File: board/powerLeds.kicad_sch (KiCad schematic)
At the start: 6 parts

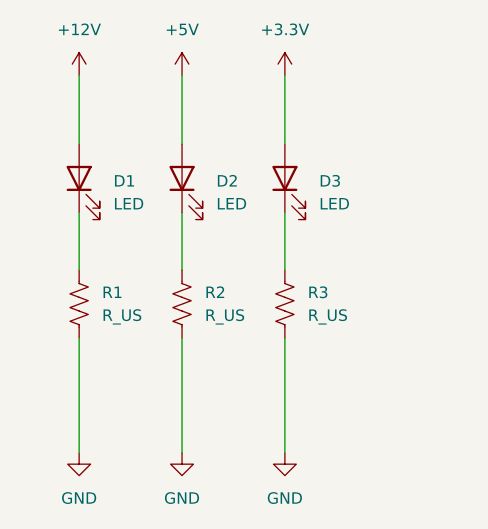
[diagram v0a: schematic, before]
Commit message: Added Resistors to Power LED's
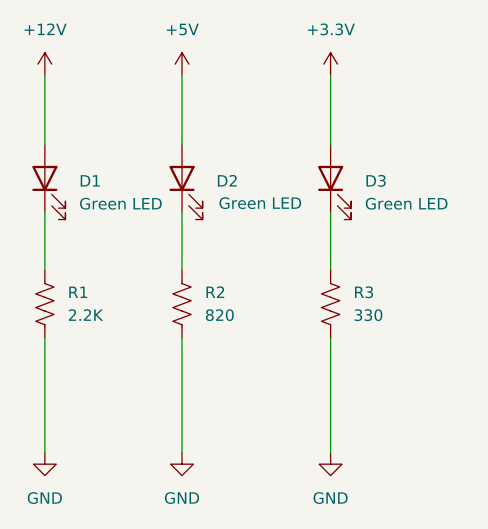
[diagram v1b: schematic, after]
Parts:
- D1, D2, D3: value LED -> Green LED
- R1: value R_US -> 2.2K
- R2: value R_US -> 820
- R3: value R_US -> 330
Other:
- moved on the sheet: D1, D3, R1, R3
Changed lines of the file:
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@@
 	(wire
 		(pts
-			(xy 127 82.55) (xy 127 90.17)
+			(xy 123.19 82.55) (xy 123.19 90.17)
 		)
 		(stroke
@@
 	(wire
 		(pts
-			(xy 127 111.76) (xy 127 124.46)
+			(xy 123.19 111.76) (xy 123.19 124.46)
 		)
 		(stroke
@@
 	(wire
 		(pts
-			(xy 149.86 97.79) (xy 149.86 104.14)
+			(xy 154.94 97.79) (xy 154.94 104.14)
 		)
 		(stroke
@@
 	(wire
 		(pts
-			(xy 149.86 82.55) (xy 149.86 90.17)
+			(xy 154.94 82.55) (xy 154.94 90.17)
 		)
 		(stroke
@@
 	(wire
 		(pts
-			(xy 149.86 111.76) (xy 149.86 124.46)
+			(xy 154.94 111.76) (xy 154.94 124.46)
 		)
 		(stroke
@@
 	(wire
 		(pts
-			(xy 127 97.79) (xy 127 104.14)
+			(xy 123.19 97.79) (xy 123.19 104.14)
 		)
 		(stroke
@@
 	(symbol
 		(lib_id "power:+12V")
-		(at 127 82.55 0)
+		(at 123.19 82.55 0)
 		(unit 1)
 		(exclude_from_sim no)
@@
 		(fields_autoplaced yes)
 		(property "Reference" "#PWR04"
-			(at 127 86.36 0)
+			(at 123.19 86.36 0)
 			(effects
 				(font
@@
 		)
 		(property "Value" "+12V"
-			(at 127 77.47 0)
-			(effects
-				(font
-					(size 1.27 1.27)
-				)
-			)
-		)
-		(property "Footprint" ""
-			(at 127 82.55 0)
+			(at 123.19 77.47 0)
+			(effects
+				(font
+					(size 1.27 1.27)
+				)
+			)
+		)
+		(property "Footprint" ""
+			(at 123.19 82.55 0)
 			(effects
 				(font
@@
 		)
 		(property "Datasheet" ""
-			(at 127 82.55 0)
+			(at 123.19 82.55 0)
 			(effects
 				(font
@@
 		)
 		(property "Description" "Power symbol creates a global label with name \"+12V\""
-			(at 127 82.55 0)
+			(at 123.19 82.55 0)
 			(effects
 				(font
@@
 	(symbol
 		(lib_id "Device:LED")
-		(at 127 93.98 90)
+		(at 123.19 93.98 90)
 		(unit 1)
 		(exclude_from_sim no)
@@
 		(fields_autoplaced yes)
 		(property "Reference" "D1"
-			(at 130.81 94.2974 90)
+			(at 127 94.2974 90)
 			(effects
 				(font
@@
 			)
 		)
-		(property "Value" "LED"
-			(at 130.81 96.8374 90)
+		(property "Value" "Green LED"
+			(at 127 96.8374 90)
 			(effects
 				(font
@@
 		)
 		(property "Footprint" ""
-			(at 127 93.98 0)
+			(at 123.19 93.98 0)
 			(effects
 				(font
@@
 		)
 		(property "Datasheet" "~"
-			(at 127 93.98 0)
+			(at 123.19 93.98 0)
 			(effects
 				(font
@@
 		)
 		(property "Description" "Light emitting diode"
-			(at 127 93.98 0)
+			(at 123.19 93.98 0)
 			(effects
 				(font
@@
 		)
 		(property "Sim.Pins" "1=K 2=A"
-			(at 127 93.98 0)
+			(at 123.19 93.98 0)
 			(effects
 				(font
@@
 		(on_board yes)
 		(dnp no)
-		(fields_autoplaced yes)
 		(property "Reference" "D2"
 			(at 142.24 94.2974 90)
@@
 			)
 		)
-		(property "Value" "LED"
-			(at 142.24 96.8374 90)
+		(property "Value" "Green LED"
+			(at 142.494 96.774 90)
 			(effects
 				(font
@@
 	(symbol
 		(lib_id "Device:R_US")
-		(at 149.86 107.95 0)
+		(at 154.94 107.95 0)
 		(unit 1)
 		(exclude_from_sim no)
@@
 		(fields_autoplaced yes)
 		(property "Reference" "R3"
-			(at 152.4 106.6799 0)
+			(at 157.48 106.6799 0)
 			(effects
 				(font
@@
 			)
 		)
-		(property "Value" "R_US"
-			(at 152.4 109.2199 0)
+		(property "Value" "330"
+			(at 157.48 109.2199 0)
 			(effects
 				(font
@@
 		)
 		(property "Footprint" ""
-			(at 150.876 108.204 90)
+			(at 155.956 108.204 90)
 			(effects
 				(font
@@
 		)
 		(property "Datasheet" "~"
-			(at 149.86 107.95 0)
+			(at 154.94 107.95 0)
 			(effects
 				(font
@@
 		)
 		(property "Description" "Resistor, US symbol"
-			(at 149.86 107.95 0)
+			(at 154.94 107.95 0)
 			(effects
 				(font
@@
 	(symbol
 		(lib_id "Device:LED")
-		(at 149.86 93.98 90)
+		(at 154.94 93.98 90)
 		(unit 1)
 		(exclude_from_sim no)
@@
 		(fields_autoplaced yes)
 		(property "Reference" "D3"
-			(at 153.67 94.2974 90)
+			(at 158.75 94.2974 90)
 			(effects
 				(font
@@
 			)
 		)
-		(property "Value" "LED"
-			(at 153.67 96.8374 90)
+		(property "Value" "Green LED"
+			(at 158.75 96.8374 90)
 			(effects
 				(font
@@
 		)
 		(property "Footprint" ""
-			(at 149.86 93.98 0)
+			(at 154.94 93.98 0)
 			(effects
 				(font
@@
 		)
 		(property "Datasheet" "~"
-			(at 149.86 93.98 0)
+			(at 154.94 93.98 0)
 			(effects
 				(font
@@
 		)
 		(property "Description" "Light emitting diode"
-			(at 149.86 93.98 0)
+			(at 154.94 93.98 0)
 			(effects
 				(font
@@
 		)
 		(property "Sim.Pins" "1=K 2=A"
-			(at 149.86 93.98 0)
+			(at 154.94 93.98 0)
 			(effects
 				(font
@@
 			)
 		)
-		(property "Value" "R_US"
+		(property "Value" "820"
 			(at 140.97 109.2199 0)
 			(effects
@@
 	(symbol
 		(lib_id "power:GND")
-		(at 127 124.46 0)
+		(at 123.19 124.46 0)
 		(unit 1)
 		(exclude_from_sim no)
@@
 		(fields_autoplaced yes)
 		(property "Reference" "#PWR07"
-			(at 127 130.81 0)
+			(at 123.19 130.81 0)
 			(effects
 				(font
@@
 		)
 		(property "Value" "GND"
-			(at 127 129.54 0)
-			(effects
-				(font
-					(size 1.27 1.27)
-				)
-			)
-		)
-		(property "Footprint" ""
-			(at 127 124.46 0)
+			(at 123.19 129.54 0)
+			(effects
+				(font
+					(size 1.27 1.27)
+				)
+			)
+		)
+		(property "Footprint" ""
+			(at 123.19 124.46 0)
 			(effects
 				(font
@@
 		)
 		(property "Datasheet" ""
-			(at 127 124.46 0)
+			(at 123.19 124.46 0)
 			(effects
 				(font
@@
 		)
 		(property "Description" "Power symbol creates a global label with name \"GND\" , ground"
-			(at 127 124.46 0)
+			(at 123.19 124.46 0)
 			(effects
 				(font
@@
 	(symbol
 		(lib_id "Device:R_US")
-		(at 127 107.95 0)
+		(at 123.19 107.95 0)
 		(unit 1)
 		(exclude_from_sim no)
@@
 		(fields_autoplaced yes)
 		(property "Reference" "R1"
-			(at 129.54 106.6799 0)
+			(at 125.73 106.6799 0)
 			(effects
 				(font
@@
 			)
 		)
-		(property "Value" "R_US"
-			(at 129.54 109.2199 0)
+		(property "Value" "2.2K"
+			(at 125.73 109.2199 0)
 			(effects
 				(font
@@
 		)
 		(property "Footprint" ""
-			(at 128.016 108.204 90)
+			(at 124.206 108.204 90)
 			(effects
 				(font
@@
 		)
 		(property "Datasheet" "~"
-			(at 127 107.95 0)
+			(at 123.19 107.95 0)
 			(effects
 				(font
@@
 		)
 		(property "Description" "Resistor, US symbol"
-			(at 127 107.95 0)
+			(at 123.19 107.95 0)
 			(effects
 				(font
@@
 	(symbol
 		(lib_id "power:GND")
-		(at 149.86 124.46 0)
+		(at 154.94 124.46 0)
 		(unit 1)
 		(exclude_from_sim no)
@@
 		(fields_autoplaced yes)
 		(property "Reference" "#PWR09"
-			(at 149.86 130.81 0)
+			(at 154.94 130.81 0)
 			(effects
 				(font
@@
 		)
 		(property "Value" "GND"
-			(at 149.86 129.54 0)
-			(effects
-				(font
-					(size 1.27 1.27)
-				)
-			)
-		)
-		(property "Footprint" ""
-			(at 149.86 124.46 0)
+			(at 154.94 129.54 0)
+			(effects
+				(font
+					(size 1.27 1.27)
+				)
+			)
+		)
+		(property "Footprint" ""
+			(at 154.94 124.46 0)
 			(effects
 				(font
@@
 		)
 		(property "Datasheet" ""
-			(at 149.86 124.46 0)
+			(at 154.94 124.46 0)
 			(effects
 				(font
@@
 		)
 		(property "Description" "Power symbol creates a global label with name \"GND\" , ground"
-			(at 149.86 124.46 0)
+			(at 154.94 124.46 0)
 			(effects
 				(font
@@
 	(symbol
 		(lib_id "power:+3.3V")
-		(at 149.86 82.55 0)
+		(at 154.94 82.55 0)
 		(unit 1)
 		(exclude_from_sim no)
@@
 		(fields_autoplaced yes)
 		(property "Reference" "#PWR06"
-			(at 149.86 86.36 0)
+			(at 154.94 86.36 0)
 			(effects
 				(font
@@
 		)
 		(property "Value" "+3.3V"
-			(at 149.86 77.47 0)
-			(effects
-				(font
-					(size 1.27 1.27)
-				)
-			)
-		)
-		(property "Footprint" ""
-			(at 149.86 82.55 0)
+			(at 154.94 77.47 0)
+			(effects
+				(font
+					(size 1.27 1.27)
+				)
+			)
+		)
+		(property "Footprint" ""
+			(at 154.94 82.55 0)
 			(effects
 				(font
@@
 		)
 		(property "Datasheet" ""
-			(at 149.86 82.55 0)
+			(at 154.94 82.55 0)
 			(effects
 				(font
@@
 		)
 		(property "Description" "Power symbol creates a global label with name \"+3.3V\""
-			(at 149.86 82.55 0)
-			(effects
-				(font
+			(at 154.94 82.55 0)
+			(effects
+				(font
